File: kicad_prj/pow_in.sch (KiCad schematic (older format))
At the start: 13 parts

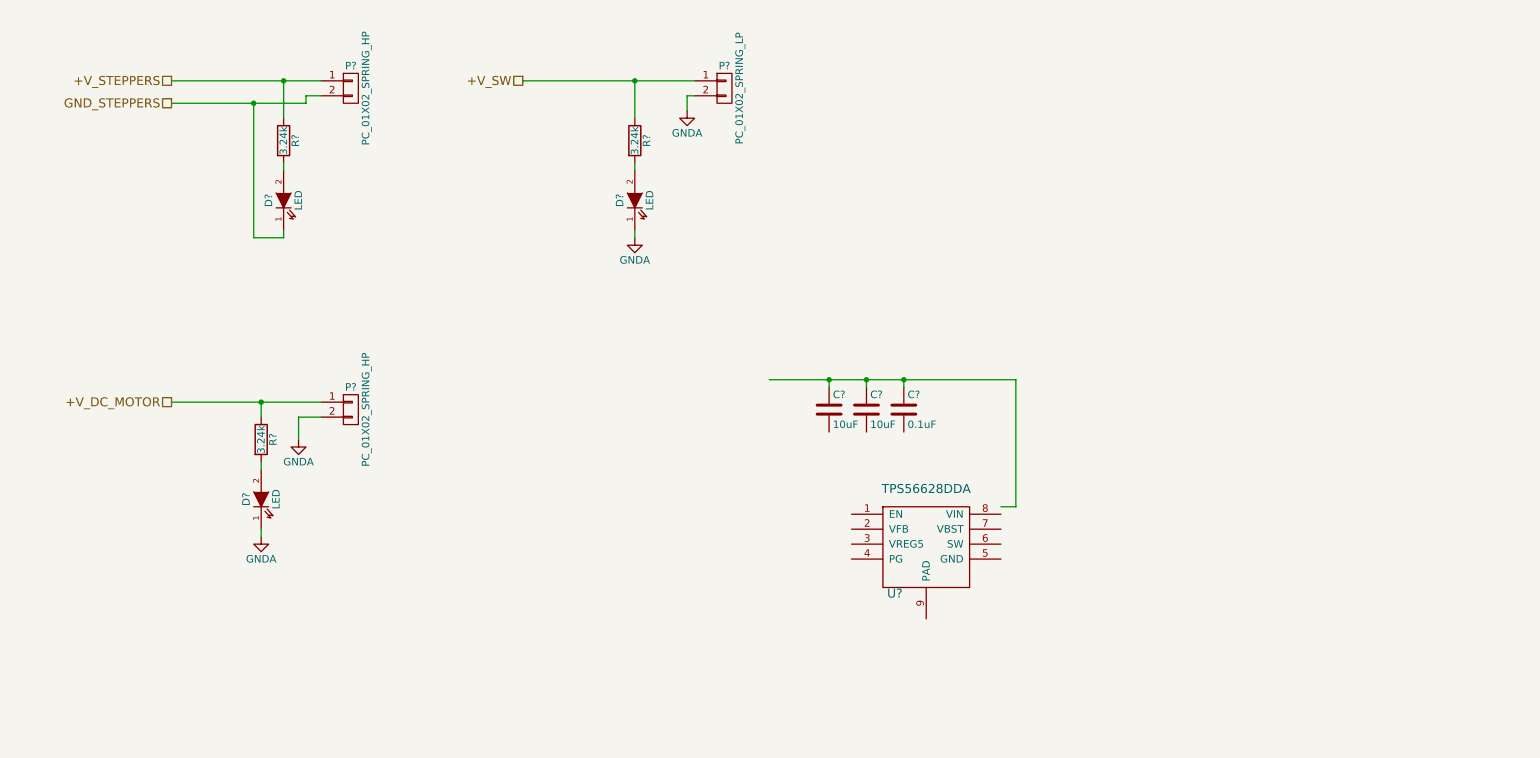
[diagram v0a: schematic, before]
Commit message: Schematics 8
Power for power side is finished. Need to add switching converter for
3.3V isolated side.
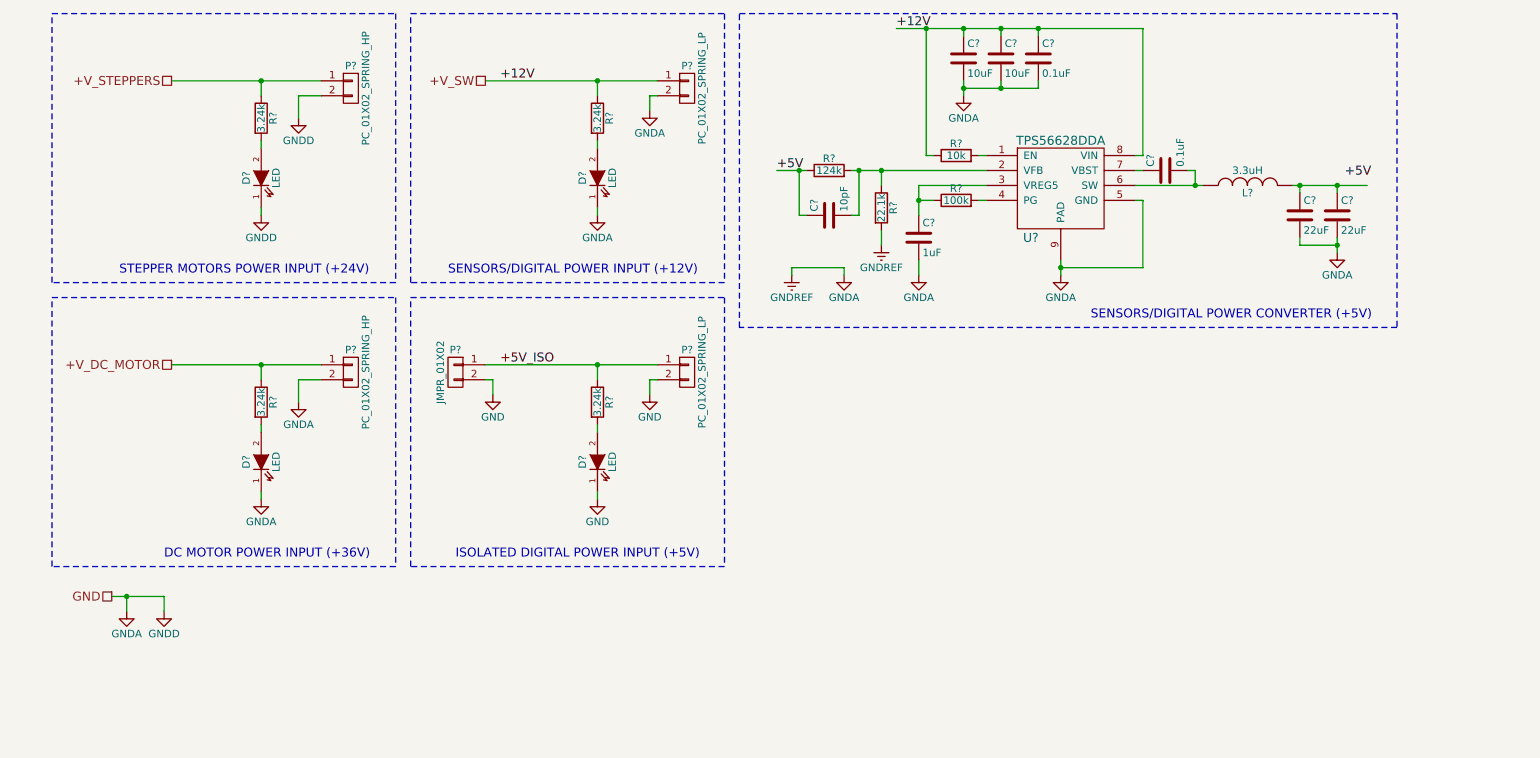
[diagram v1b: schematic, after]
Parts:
- removed D?: LED, symbol LED
- removed P?: PC_01X02_SPRING_HP, symbol PC_01X02_SPRING_HP
- removed R?: 3.24k, symbol R
- removed U?: TPS56628DDA, symbol TPS56628DDA
- added C? (x2): 22uF, symbol C
- added C?: 1uF, symbol C
- added C?: 10pF, symbol C
- added C?: 0.1uF, symbol C
- added D? (x2): LED, symbol LED
- added L?: 3.3uH, symbol L
- added P?: PC_01X02_SPRING_LP, symbol PC_01X02_SPRING_LP
- added P?: PC_01X02_SPRING_HP, symbol PC_01X02_SPRING_HP
- added P?: JMPR_01X02, symbol JMPR_01X02
- added R?: 100k, symbol R
- added R?: 22.1k, symbol R
- added R?: 124k, symbol R
- added R?: 10k, symbol R
- added R? (x2): 3.24k, symbol R
- added U?: TPS56628DDA, symbol TPS56628DDA
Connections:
- net labels added: +12V, +5V, +5V_ISO, GND, GNDD, GNDREF
- net labels removed: GND_STEPPERS
- wire segments 27 -> 92
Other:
- note added: "DC MOTOR POWER INPUT (+36V)"
- note added: "ISOLATED DIGITAL POWER INPUT (+5V)"
- note added: "SENSORS/DIGITAL POWER CONVERTER (+5V)"
- note added: "SENSORS/DIGITAL POWER INPUT (+12V)"
- note added: "STEPPER MOTORS POWER INPUT (+24V)"
- moved on the sheet: C?, D?, P?, R?

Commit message: Schematics 9
Power circuitry is done.
Need to do MCU circuitry and top level connections.
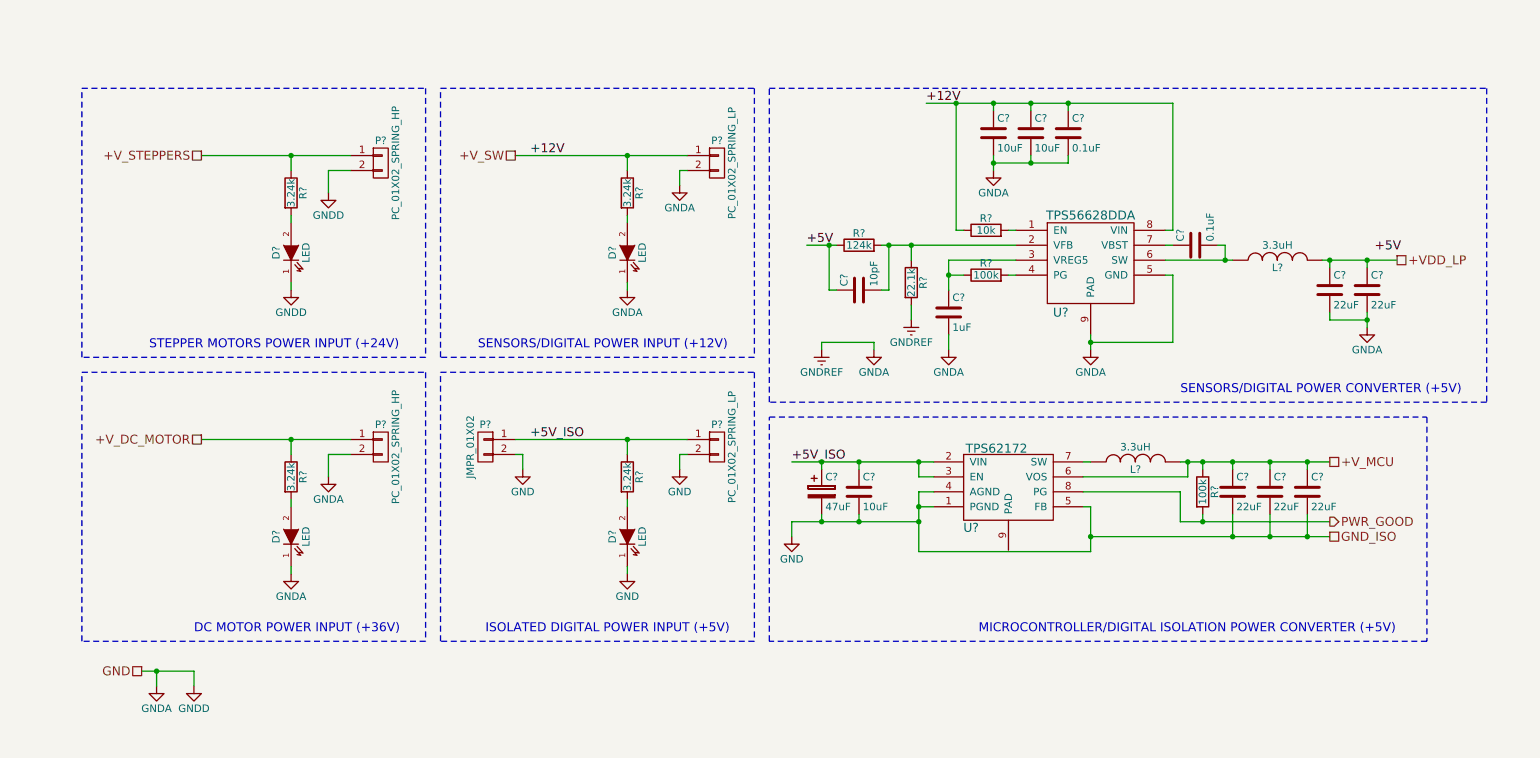
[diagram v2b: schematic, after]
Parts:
- added C? (x3): 22uF, symbol C
- added C?: 10uF, symbol C
- added C?: 47uF, symbol CP
- added L?: 3.3uH, symbol L
- added R?: 100k, symbol R
- added U?: TPS62172, symbol TPS62172
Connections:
- net +5V_ISO: now also C?.1, C?.1, U?.2 (VIN), U?.3 (EN)
- net GND: now also C?.2, C?.2, C?.2, C?.2, C?.2, U?.1 (PGND), U?.4 (AGND), U?.5 (FB)
- net +VDD_LP: now reaches C?.1, C?.1, L?.2
- new net: L?.1, U?.7 (SW)
- new net +V_MCU: C?.1, C?.1, C?.1, L?.2, R?.1, U?.6 (VOS)
- new net PWR_GOOD: R?.2, U?.8 (PG)
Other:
- note added: "MICROCONTROLLER/DIGITAL ISOLATION POWER CONVERTER (+5V)"
- moved on the sheet: C?, D?, L?, P?, R?, U?

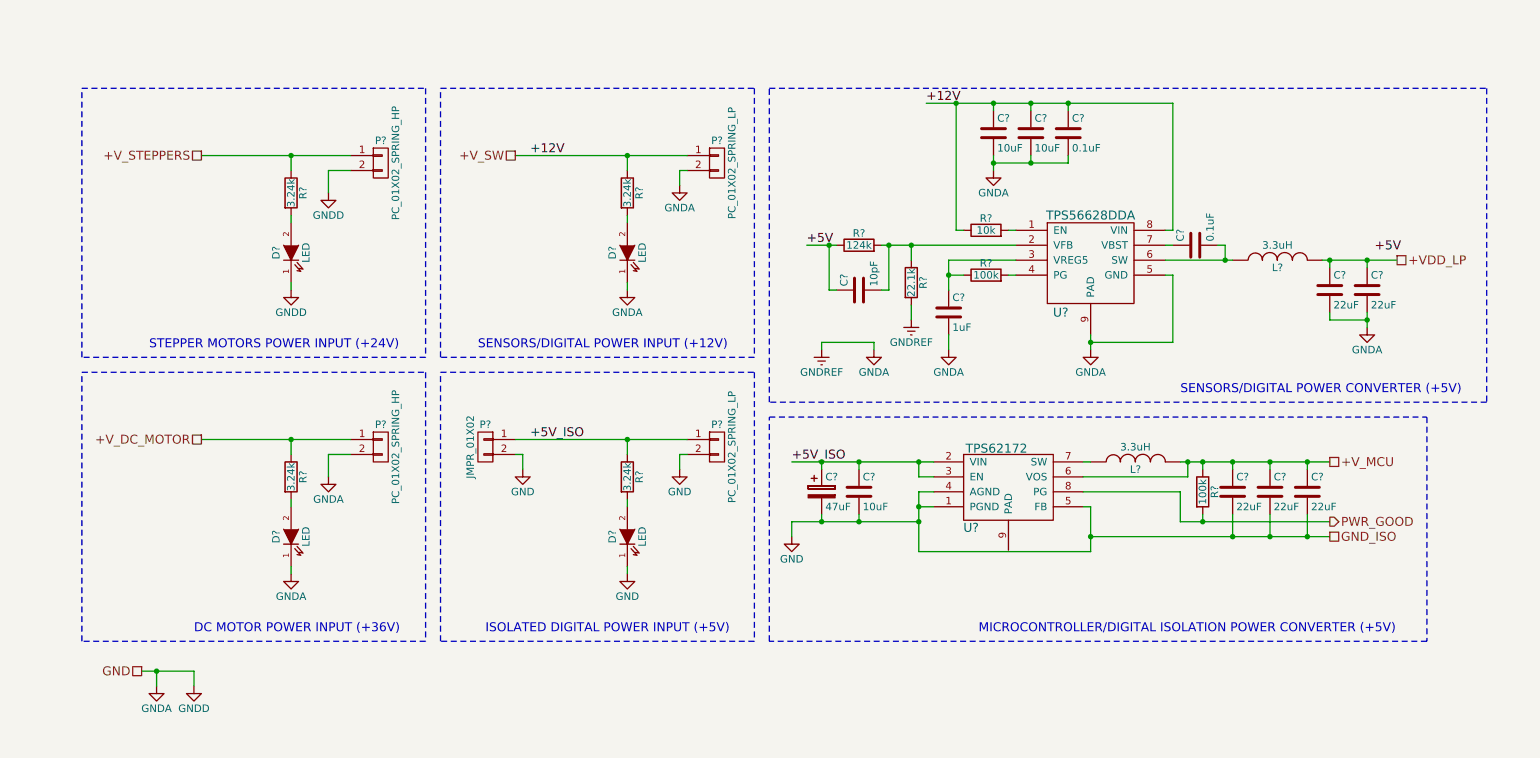
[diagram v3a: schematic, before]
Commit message: Corrected sheet sizes
A4 to A size on all sheets
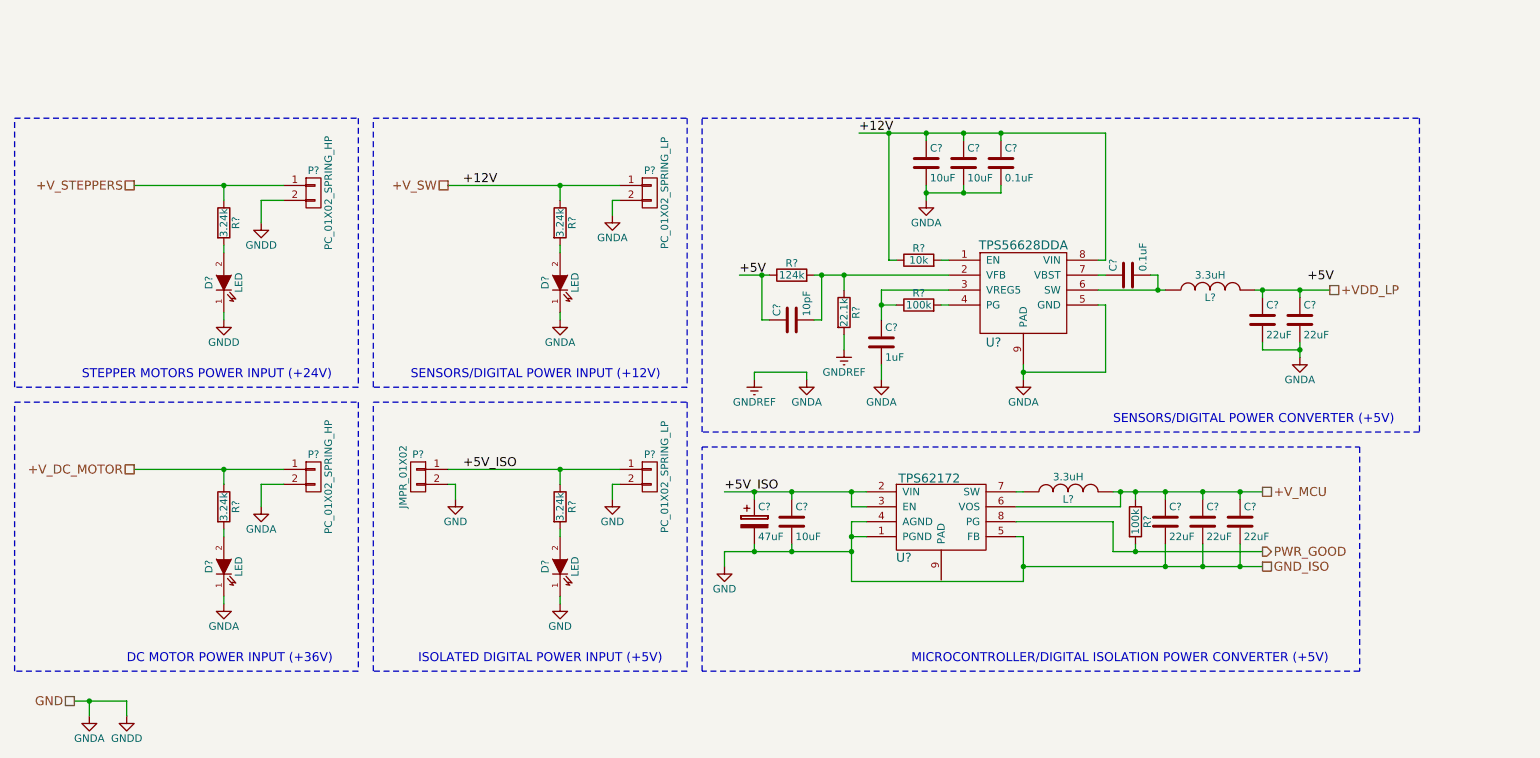
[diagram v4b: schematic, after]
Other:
- moved on the sheet: C?, D?, L?, P?, R?, U?
